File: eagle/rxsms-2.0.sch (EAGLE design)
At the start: 149 parts, among them Q1 opt, Q10 BSS123, Q11 BSS123, Q12 BSS123, Q2 BSS123, Q3 BSS123, Q4 BSS123, Q5 BSS123, Q6 BSS123, Q7 BSS123, Q8 BSS123, Q9 BSS123, T1 SMS_IP67, T10 SWITCH_LED, T2 SMS_IP67, T3 SWITCH_LED, T4 SMS_IP67, T5 SMS_IP67, T6 SWITCH_LED, T7 SWITCH_LED, T8 SWITCH_LED, T9 SMS_IP67, U1 MAX3232ESE, U2 XMEGA-A4UTQFP, U3 TSR_1-2450, U4 LM1117, U5 TMV_0505EN, U6 ADUM3160, U7 TPS73125, U8 NUP2202W1, X1 PN61729-S, X5 RLP2-200-500

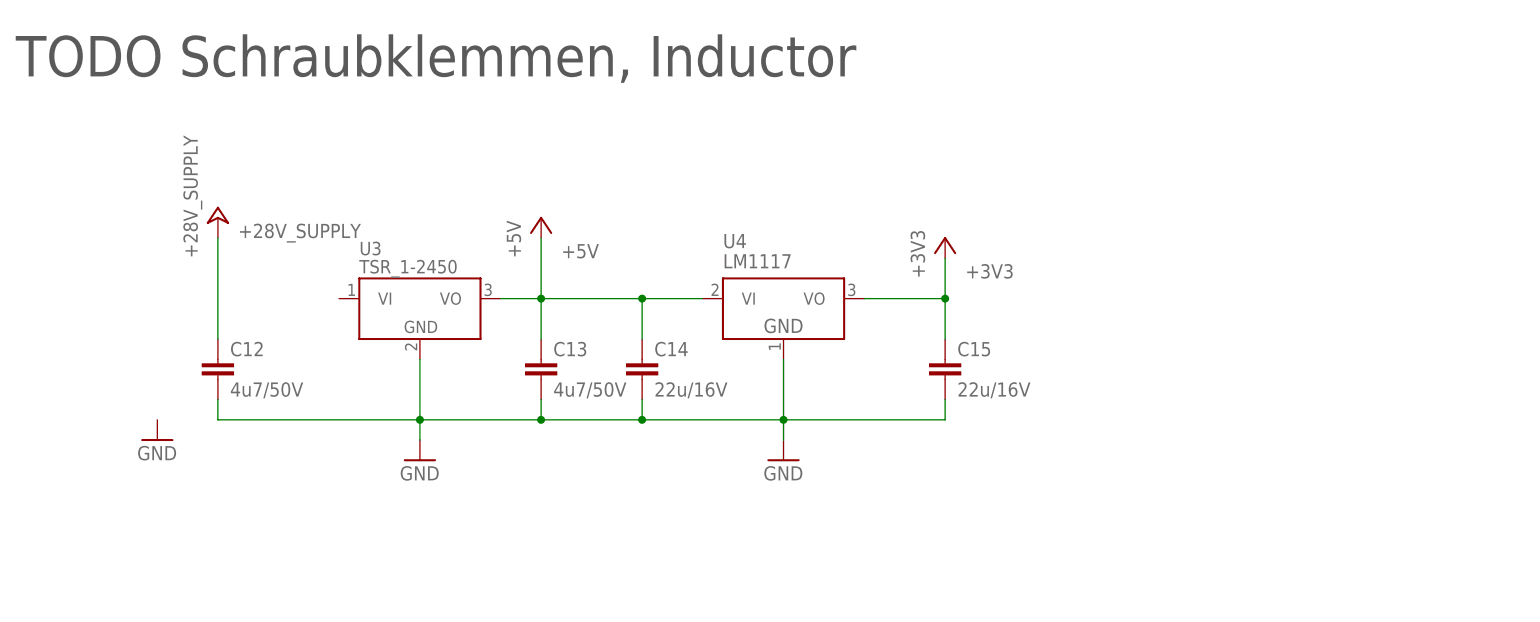
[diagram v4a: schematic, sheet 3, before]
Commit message: minor cleanup, TODOs updated
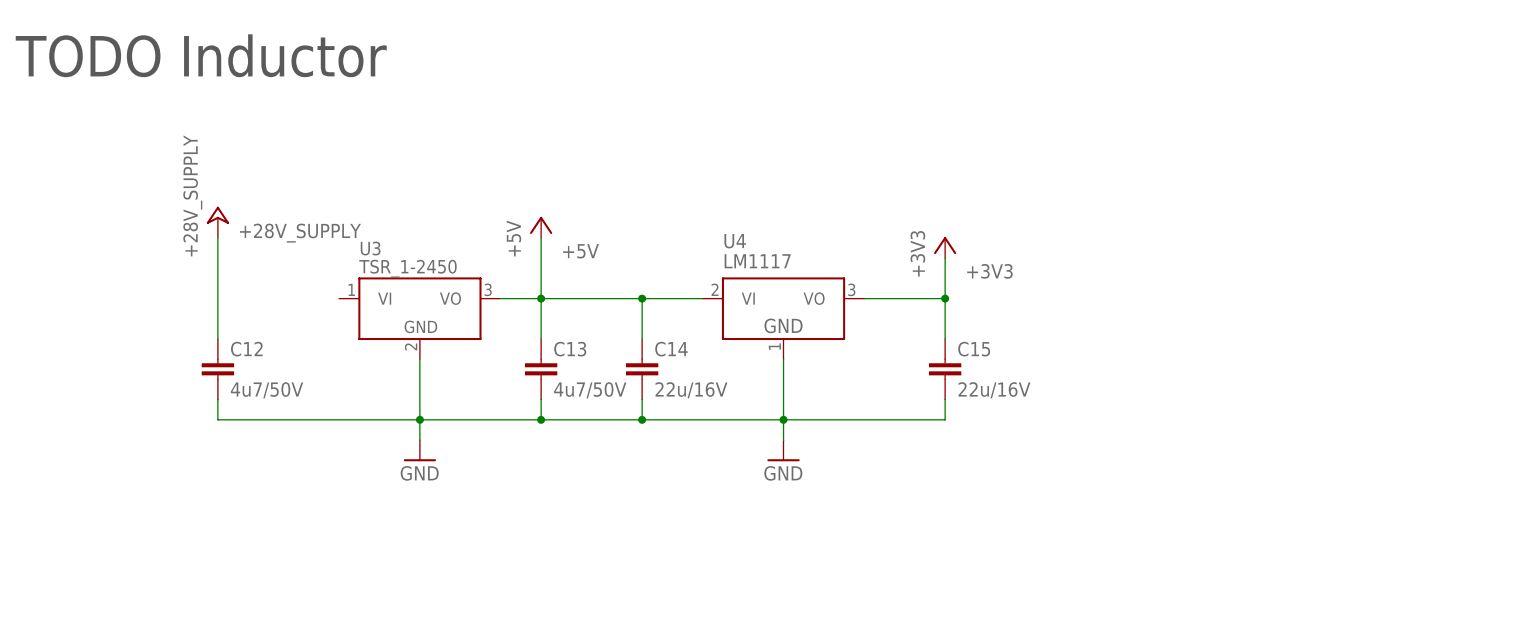
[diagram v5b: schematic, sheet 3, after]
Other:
- note added: "TODO Inductor"
- note removed: "TODO Schraubklemmen, Inductor"
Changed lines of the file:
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@@
 <part name="GND6" library="supply1" deviceset="GND" device=""/>
 <part name="P+2" library="supply1" deviceset="+24V" device="" value="+28V_SUPPLY"/>
-<part name="GND7" library="supply1" deviceset="GND" device=""/>
 <part name="P+3" library="supply1" deviceset="+5V" device=""/>
 <part name="C14" library="rcl" deviceset="C-EU" device="C0805K" value="22u/16V"/>
@@
 <sheet>
 <plain>
-<text x="27.94" y="152.4" size="5.08" layer="97">TODO Schraubklemmen, Inductor</text>
+<text x="27.94" y="152.4" size="5.08" layer="97">TODO Inductor</text>
 </plain>
 <instances>
@@
 <instance part="GND6" gate="1" x="124.46" y="104.14"/>
 <instance part="P+2" gate="1" x="53.34" y="134.62"/>
-<instance part="GND7" gate="1" x="45.72" y="106.68"/>
 <instance part="P+3" gate="1" x="93.98" y="134.62"/>
 <instance part="C14" gate="G$1" x="106.68" y="116.84"/>

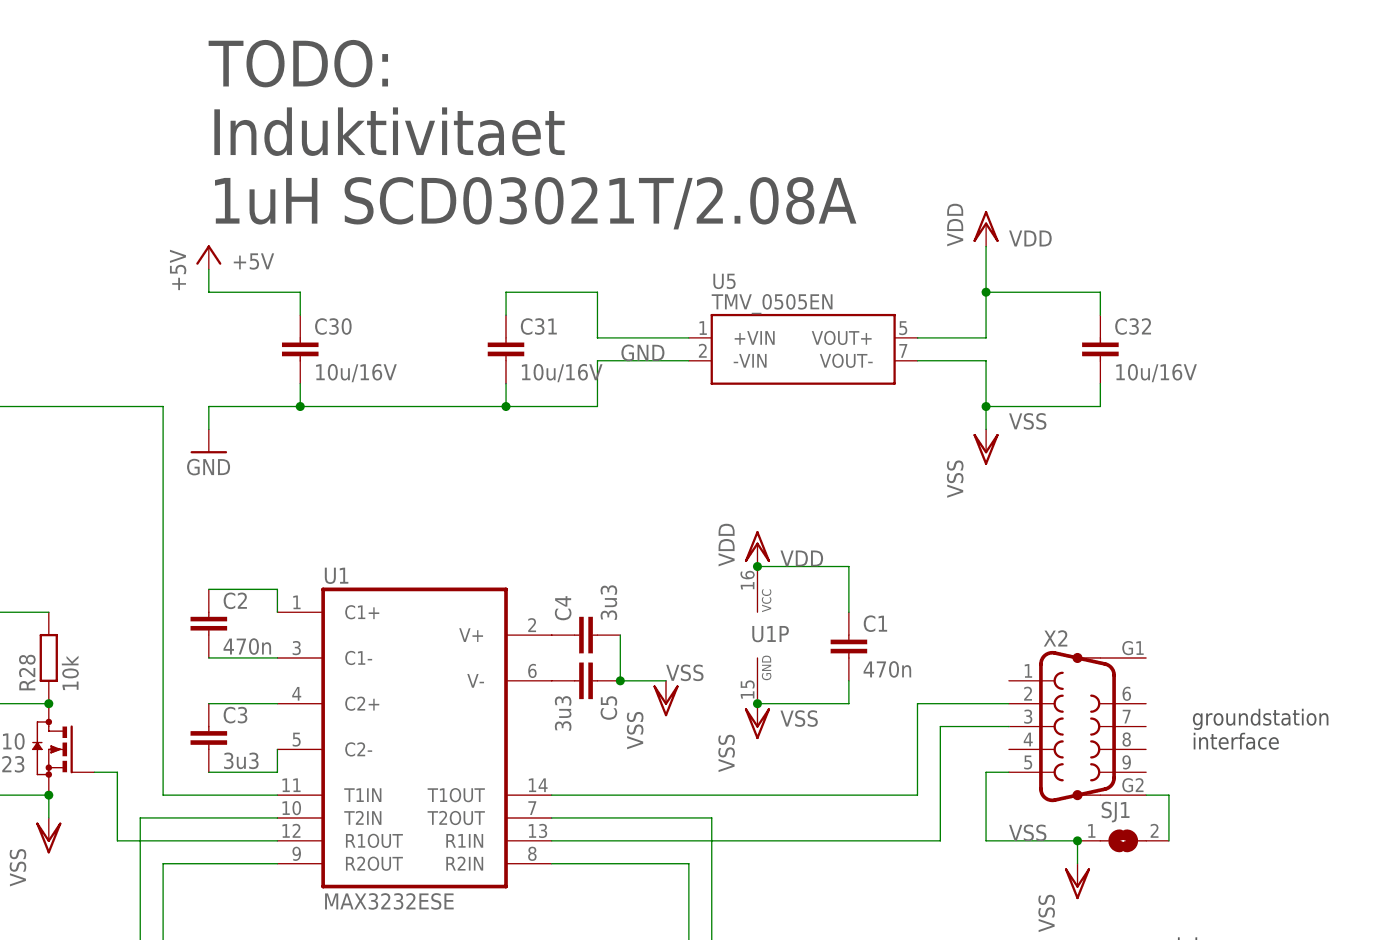
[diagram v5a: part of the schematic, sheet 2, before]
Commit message: most components selected
  * replaced unregulated TMV regulator with TES3
  * added coil library
  * added missing coils to DCDC regulators
  * added various 100nF capacitors
  * added jumper between USB shield and RC filter
  * operate MAX3232 at 3.3V and use matching capacitors
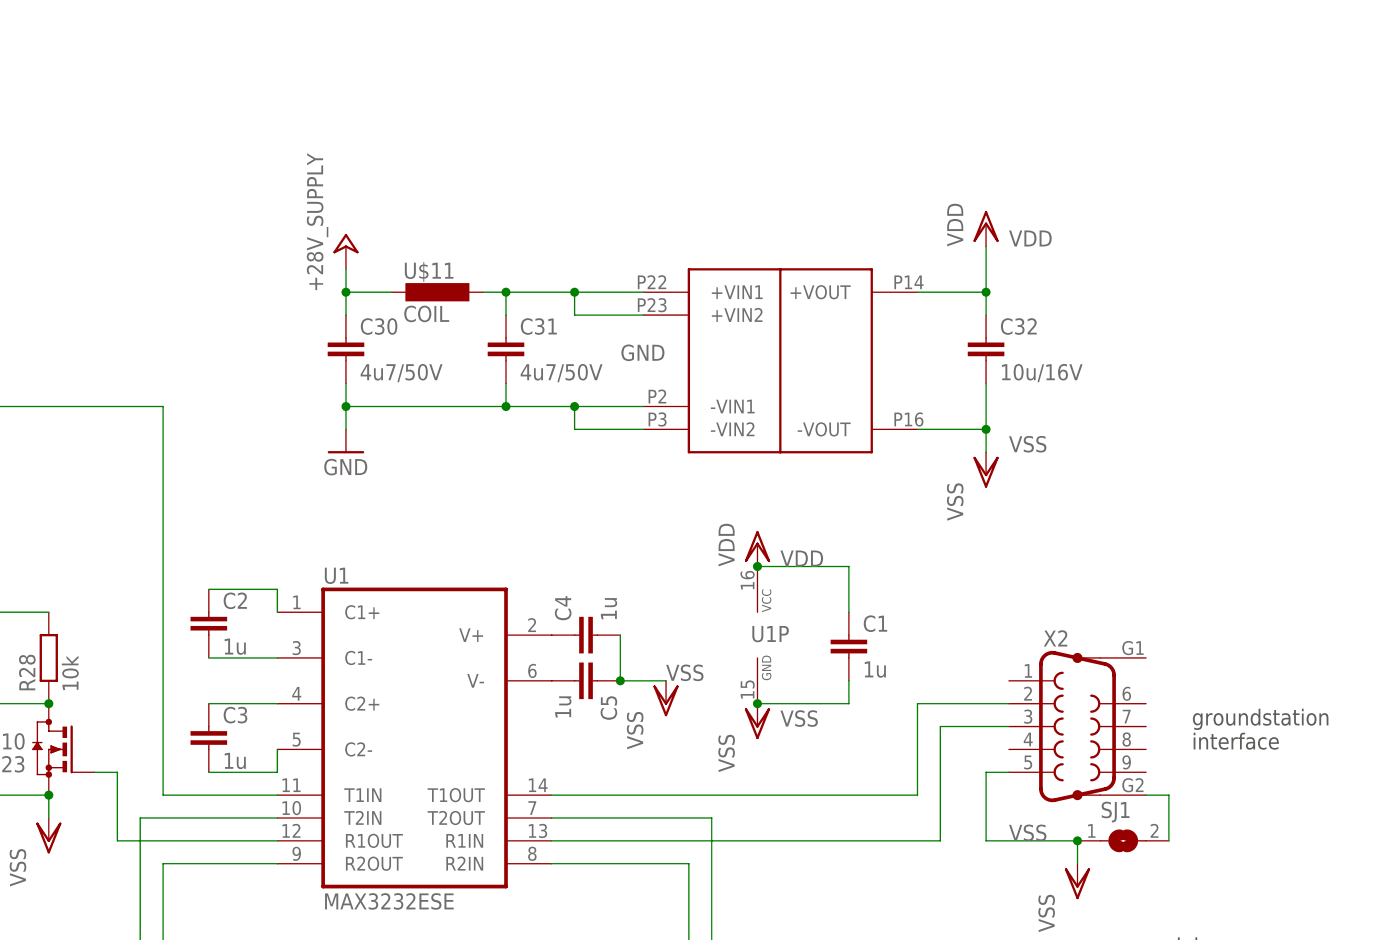
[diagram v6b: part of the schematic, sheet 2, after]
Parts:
- removed U5: TMV_0505EN, _traco_tmv-1:TMV_EN-
- added C35: 4u7/50V, rcl:C-EUC0805K
- added C36, C37, C38, C39: 100n, rcl:C-EUC0805K
- added SJ4: (no value), jumper:SJ
- added U$10: TES3-4810WI, TES3-4810WI:TES3-4810WI
- added U$11, U$12: COIL, Coil:COIL
- C1, C2: value 470n -> 1u
- C3, C4, C5: value 3u3 -> 1u
- C30, C31: value 10u/16V -> 4u7/50V; device rcl:C-EUC1206K -> rcl:C-EUC0805K
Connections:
- removed net +VIN: C31.1, U5.+VIN
- new net N$70: C31.1, U$10.+VIN1, U$10.+VIN2, U$11.1
- new net N$71: SJ4.2, X1.S1, X1.S2
- new net N$72: C34.2, R48.1, SJ4.1
- new net VI: C35.1, U$12.1, U3.VI
- net +28V_SUPPLY: now also C30.1, U$11.2, U$12.2
- net +3V3: now also C37.1
- net +5V: now also C36.1, C38.1; no longer C30.1
- net ADC_REF: now also C39.1
- net GND: now also C35.2, C36.2, C37.2, C38.2, C39.2, U$10.-VIN1, U$10.-VIN2; no longer U5.-VIN
- net USB_SHIELD: no longer C34.2, R48.1, X1.S1, X1.S2
- net VDD: now also U$10.+VOUT; no longer U5.VOUT+
- net VSS: now also U$10.-VOUT; no longer U5.VOUT-
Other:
- note removed: "TODO Inductor"
- note removed: "TODO: Induktivitaet 1uH SCD03021T/2.08A"
- moved on the sheet: C12, C15, C30, C32, U4, X1

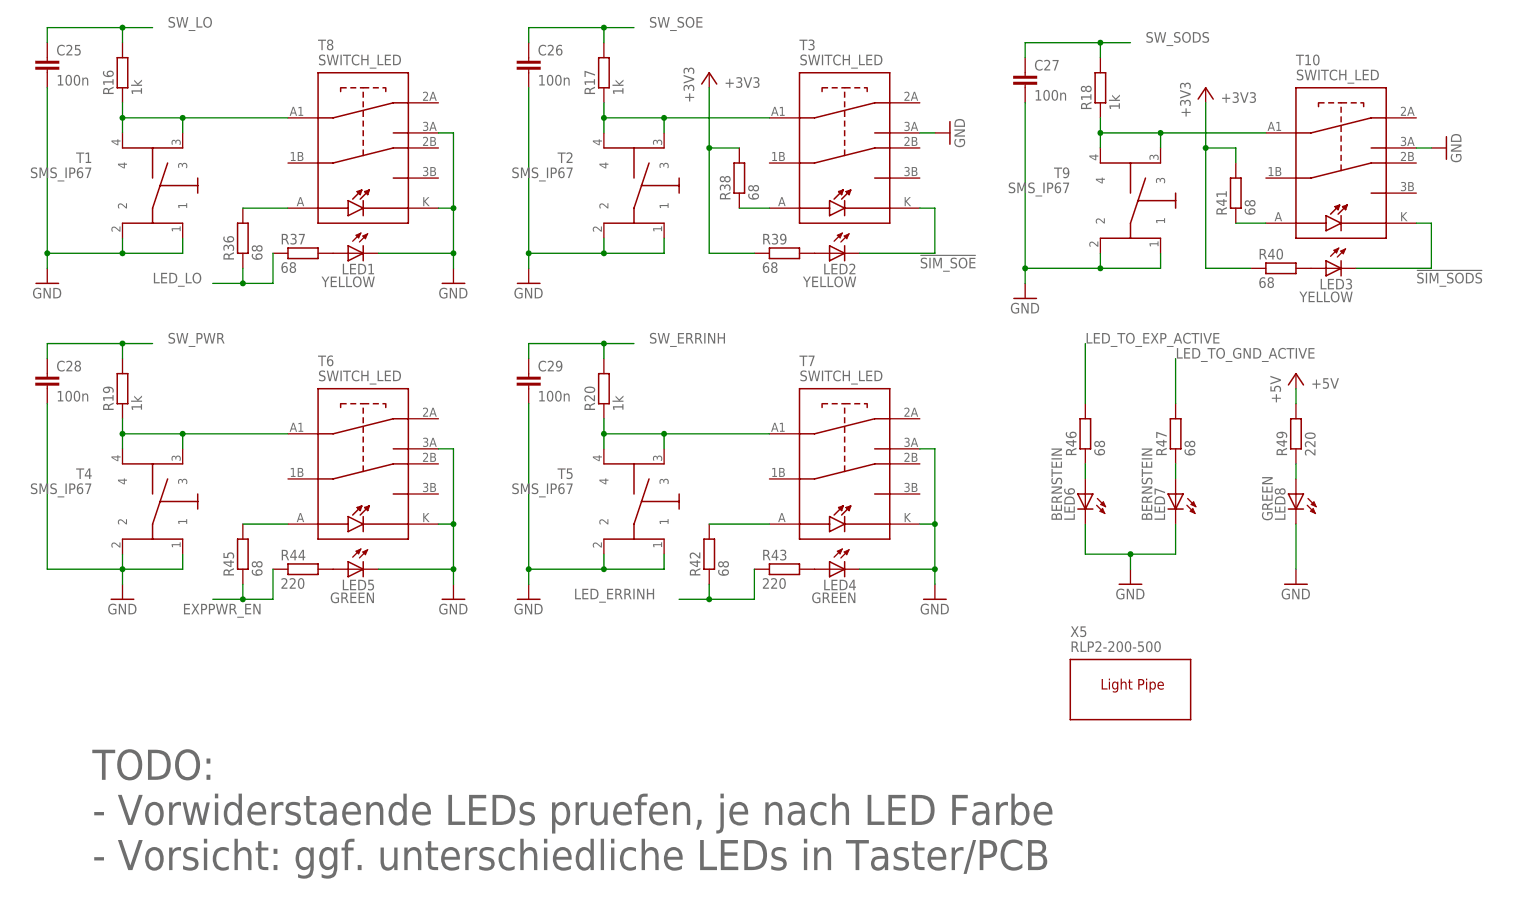
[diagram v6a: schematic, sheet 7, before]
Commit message: Placement of components acording to mechanical CAD
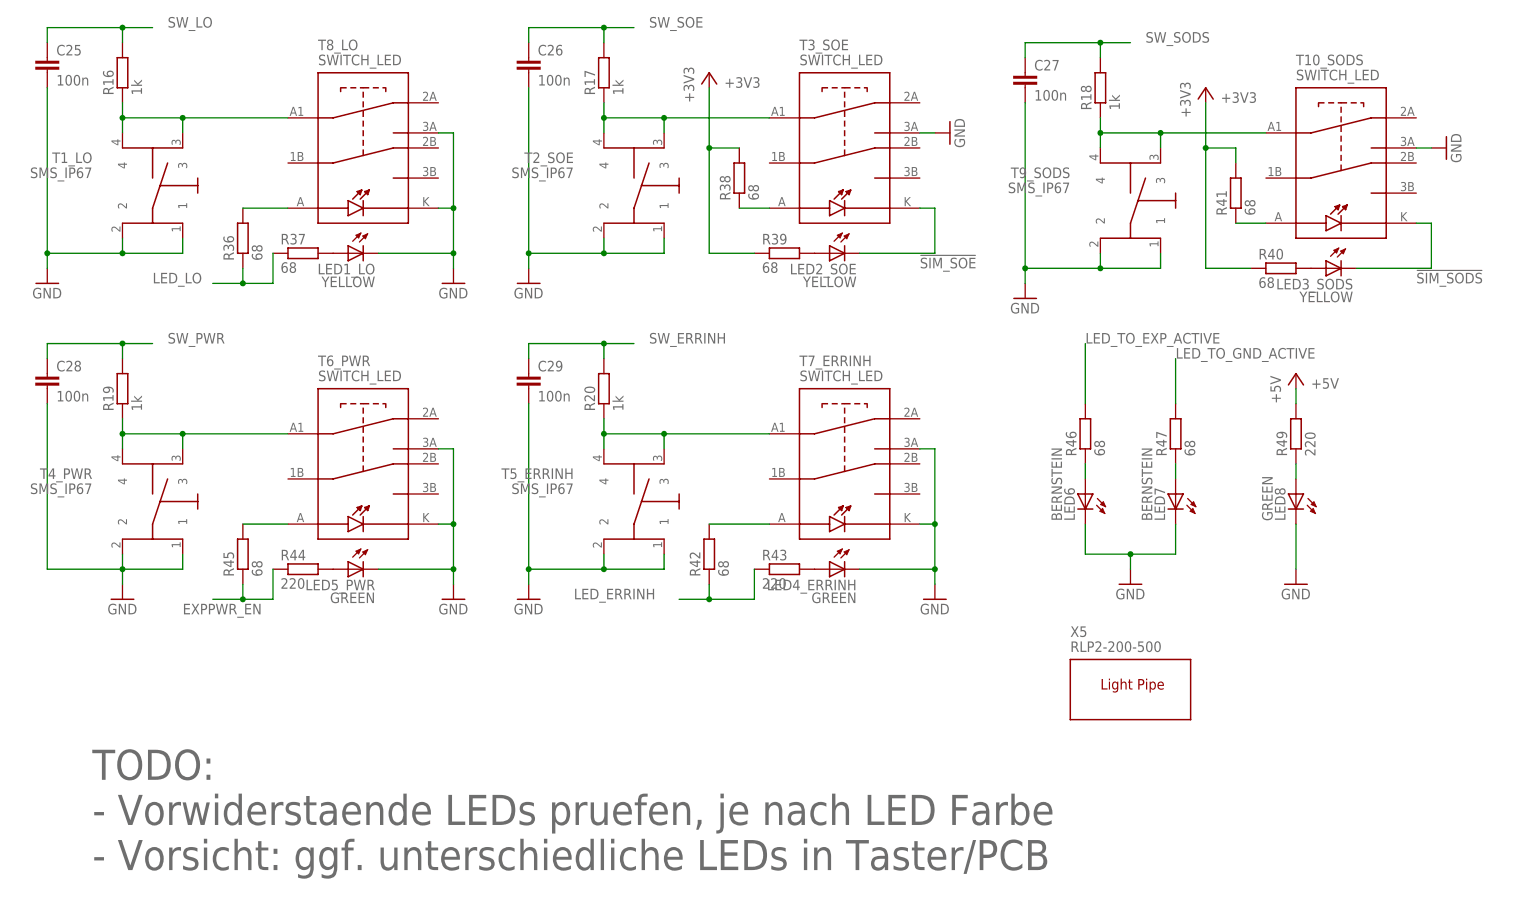
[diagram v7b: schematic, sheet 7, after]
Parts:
- renumbered LED1 to LED1_LO, LED2 to LED2_SOE, LED3 to LED3_SODS, LED4 to LED4_ERRINH, LED5 to LED5_PWR, T1 to T1_LO, T10 to T10_SODS, T2 to T2_SOE, T3 to T3_SOE, T4 to T4_PWR, T5 to T5_ERRINH, T6 to T6_PWR, T7 to T7_ERRINH, T8 to T8_LO, T9 to T9_SODS, U$7 to U$7_BER, U$8 to U$8_DROPR, U$9 to U$9_DROPDUR, X2 to X2_GROUNDSTATION, X3 to X3_DEBUG
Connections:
- net !SIM_LO: now also U2.PD0(OC0A)
- net !SIM_SODS: now also U2.PD4(OC1A/!SS!)
- net !SIM_SOE: now also U2.PD1(OC0B/XCK0)
- net DEBUG_RX_D-: now also U2.PD6(D-/RXD1/MISO)
- net DEBUG_TX_D+: now also U2.PD7(D+/TXD1/SCK)
- net EXPPWR_EN: now also U2.PD5(OC1B/XCK1/MOSI)
- net LED_ERRINH: now also U2.PC0(OC0A/!OC0ALS!/SDA)
- net LED_LO: now also U2.PC1(OC0B/OC0AHS/XCK0/SCL)
- net LED_TO_EXP_ACTIVE: now also U2.PC4(!OC0CLS!/OC1A/!SS!)
- net LED_TO_GND_ACTIVE: now also U2.PC5(OC0CHS/OC1B/XCK1/MOSI)
- net N$34: now also T3_SOE.A
- net RESERVED_UART0_RX: now also U2.PC6(!OC0DLS!/RXD1/MISO)
- net RESERVED_UART0_TX: now also U2.PC7(OC0DHS/TXD1/SCK)
- net RESERVED_UART1_RX: now also U2.PE2(OC0C/RXD0)
- net RESERVED_UART1_TX: now also U2.PE3(OC0D/TXD0)
- net SW_ERRINH: now also U2.PA6(ADC6AC1OUT)
- net SW_PWR: now also U2.PA7(ADC7/AC0OUT)
- net UART_EXP_RX: now also U2.PC2(OC0C/!OC0BLS!/RXD0)
- net UART_EXP_TX: now also U2.PC3(OC0D/OC0BHS/TXD0)
- net UART_GND_RX: now also U2.PD2(OC0C/RXD0)
- net UART_GND_TX: now also U2.PD3(OC0D/TXD0)

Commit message: continued layout
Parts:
- added C40: 100n, rcl:C-EUC0805K
- added D1: 3V, diode:ZENER-DIODESOT23
- added U5: NC7WZ17P6X, NC7WZ17:NC7WZ17P6X
- R4: value 10k -> 22k
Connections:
- removed net N$69: SV1.11, SV1.13, SV1.3, SV1.5, SV1.7, SV1.9
- removed net N$71: SJ4.2, X1.S1, X1.S2
- removed net N$72: C34.2, R48.1, SJ4.1
- new net N$73: C40.1, U5.VCC
- net !EXP_LO: now also SV1.2, U$4.OUT6; no longer U$4.OUT7
- net !EXP_SODS: now also U$4.OUT8; no longer U$4.OUT6
- net !EXP_SOE: now also U$4.OUT7; no longer U$4.OUT8
- net !SIM_LO: now also D1.C, SV1.1, U5.A1; no longer U$4.IN7
- net !SIM_SODS: now also R3.1, U$4.IN8; no longer R2.1, U$4.IN6
- net !SIM_SOE: now also R2.1, U$4.IN7; no longer R3.1, U$4.IN8
- net ADC_REF: now also JP5.2
- net GND: now also C40.2, D1.A, SV1.10, SV1.11, SV1.12, SV1.13, SV1.14, SV1.3, SV1.4, SV1.5, SV1.6, SV1.7, SV1.8, SV1.9, U5.GND
- net N$56: now also X2_GROUNDSTATION.G1; no longer X2_GROUNDSTATION.G2
- net N$57: now also SJ2.1; no longer SJ2.2
- net N$58: now also X4.G1; no longer X4.G2
- net N$60: now also T10_SODS.A
- net N$67: now also U$4.IN6, U5.Y1; no longer SV1.10, SV1.12, SV1.14, SV1.4, SV1.6, SV1.8
- net RESERVED_ADC_0: now also JP5.3
- net RESERVED_ADC_1: now also JP5.4
- net USB_GND: now also SJ4.1
- net USB_SHIELD: now also C34.2, R48.1, SJ4.2, X1.S1, X1.S2
- net VSS: now also SJ2.2; no longer SJ2.1
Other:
- moved on the sheet: C16, Q3, Q4, R10, R11, R2, R3, R4, R6, R7, R8, R9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
